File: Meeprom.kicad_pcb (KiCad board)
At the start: 2 copper layers, 16 x 38 mm, 4 parts, among them J1 Tandy_100_102_200_option_rom, U1 28C256

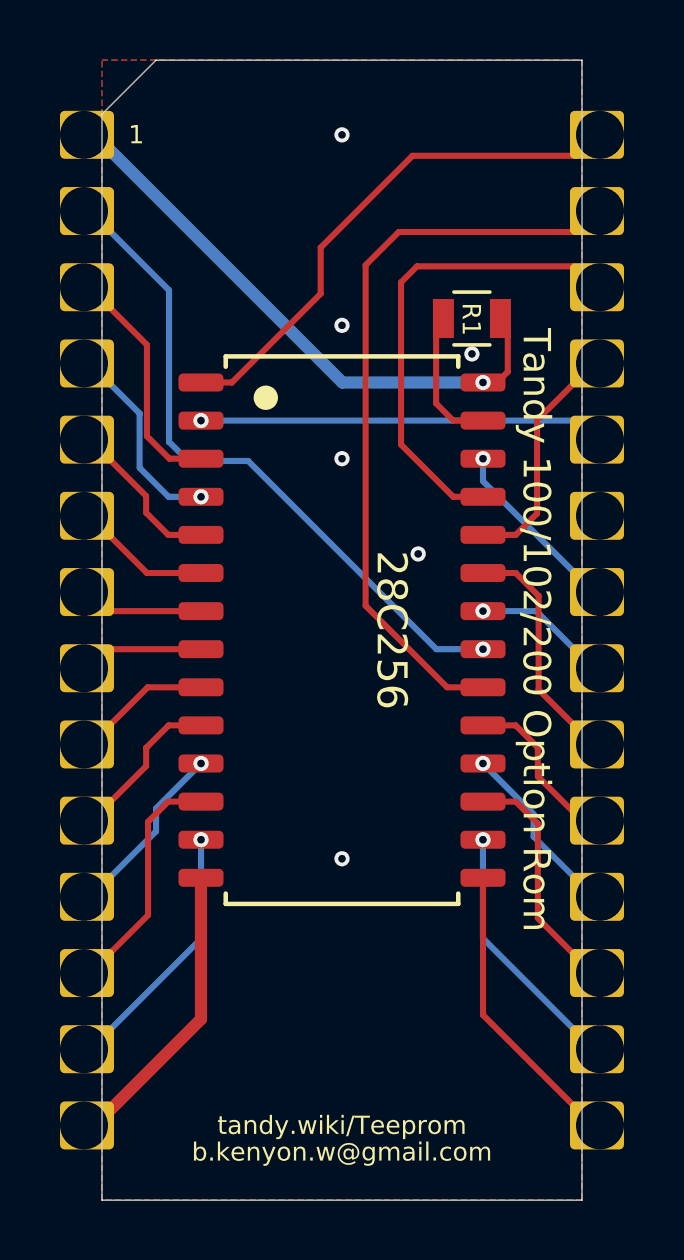
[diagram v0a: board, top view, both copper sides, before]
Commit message: Change license to CC. Add Meeprom. Add copper pours.
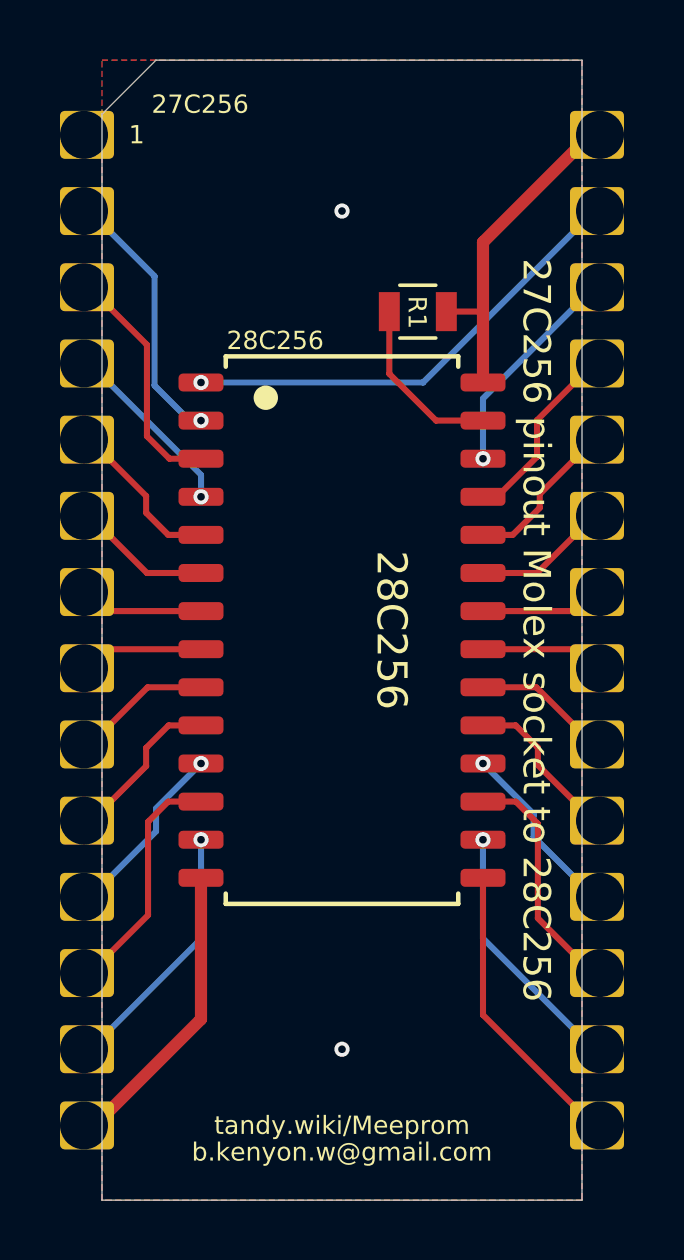
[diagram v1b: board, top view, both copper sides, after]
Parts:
- J1: value Tandy_100_102_200_option_rom -> Molex 8878 socket 27C256 pinout
- moved R1 1.82 mm to (149.7, 88.6)
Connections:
- J1 pad 1: /VCC -> (no net)
- J1 pad 2: /A10 -> /A12
- J1 pad 20: /A11 -> /~CE
- J1 pad 21: /~OE -> /A10
- J1 pad 22: /A13 -> /~OE
- J1 pad 23: (no net) -> /A11
- J1 pad 24: /A12 -> /A9
- J1 pad 25: /A9 -> /A8
- J1 pad 26: /A8 -> /A13
- J1 pad 27: /~CE -> /A14
- J1 pad 28: /A14 -> /VCC
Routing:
- net /~CE: track 24.9 -> 4.69 mm
- net /A10: track 22.2 -> 4.16 mm, vias 1 -> 0
- net /A8: track 15.9 -> 6.36 mm
- net /VCC: track 19.6 -> 11.3 mm, vias 1 -> 0
- net /A12: track 13.5 -> 8.93 mm
- net /A11: track 8.01 -> 4.69 mm
- net /A14: track 17.5 -> 15.7 mm, vias 0 -> 1
- net /A9: track 8.00 -> 6.38 mm
- net /A13: track 6.09 -> 7.44 mm
- net /~WE: track 4.73 -> 5.84 mm
- net /A6: track 6.71 -> 6.08 mm
- net /~OE: track 4.53 -> 4.16 mm, vias 1 -> 0
- net /VSS: vias 6 -> 2
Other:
- board text added: "27C256"
- board text added: "27C256 pinout Molex socket to 28C256"
- board text added: "28C256"
- board text added: "tandy.wiki/Meeprom"
- board text removed: "Tandy 100/102/200 Option Rom"
- board text removed: "tandy.wiki/Teeprom"

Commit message: improve ground paths in pours
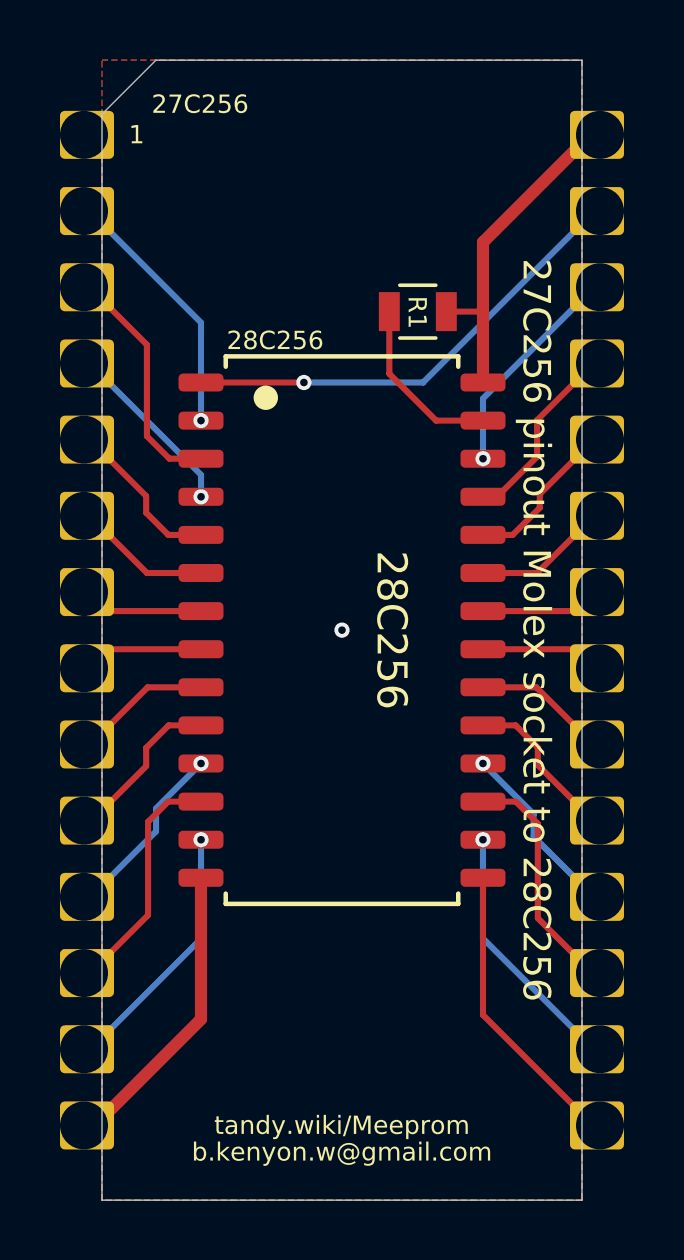
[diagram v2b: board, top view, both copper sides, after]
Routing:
- net /VSS: vias 2 -> 1
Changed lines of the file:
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@@
     (thickness 1.6)
     (drawings 13)
-    (tracks 116)
+    (tracks 114)
     (zones 0)
     (modules 4)
@@
     (add_net /~OE)
     (add_net /~WE)
-    (add_net "Net-(J1-Pad1)")
   )
   (module 000_LOCAL:pcb2molex8878_chamfer (layer Top)
@@
     (effects (font (size 0.6096 0.6096) (thickness 0.0762)) (justify left))
   )
-  (via (at 147.2184 113.157) (size 0.508) (drill 0.254) (layers Top Bottom) (net 27))
-  (via (at 147.2184 85.217) (size 0.508) (drill 0.254) (layers Top Bottom) (net 27))
   (segment (start 151.9184 112.015) (end 151.9184 107.442) (width 0.2032) (layer Top) (net 1))
   (segment (start 155.7274 115.697) (end 155.6004 115.697) (width 0.2032) (layer Top) (net 1))
@@
   (via (at 142.5184 92.202) (size 0.508) (drill 0.254) (layers Top Bottom) (net 18))
   (segment (start 138.7983 85.217) (end 138.6184 85.217) (width 0.2032) (layer Bottom) (net 18))
-  (segment (start 140.97 91.0336) (end 140.97 87.3887) (width 0.2032) (layer Bottom) (net 18))
-  (segment (start 140.97 87.3887) (end 138.7983 85.217) (width 0.2032) (layer Bottom) (net 18))
-  (segment (start 142.5184 92.202) (end 142.1384 92.202) (width 0.2032) (layer Bottom) (net 18))
-  (segment (start 142.1384 92.202) (end 140.97 91.0336) (width 0.2032) (layer Bottom) (net 18))
-  (segment (start 155.0924 92.202) (end 155.7274 92.837) (width 0.2032) (layer Bottom) (net 20))
+  (segment (start 142.5184 92.202) (end 142.5184 88.9371) (width 0.2032) (layer Bottom) (net 18))
+  (segment (start 142.5184 88.9371) (end 138.7983 85.217) (width 0.2032) (layer Bottom) (net 18))
   (via (at 142.5194 103.632) (size 0.508) (drill 0.254) (layers Top Bottom) (net 19))
   (segment (start 141.0208 105.1306) (end 142.5194 103.632) (width 0.2032) (layer Bottom) (net 19))
@@
   (segment (start 141.0208 105.8926) (end 141.0208 105.1306) (width 0.2032) (layer Bottom) (net 19))
   (segment (start 138.8364 108.077) (end 141.0208 105.8926) (width 0.2032) (layer Bottom) (net 19))
+  (segment (start 155.0924 92.202) (end 155.7274 92.837) (width 0.2032) (layer Bottom) (net 20))
   (segment (start 155.6258 92.837) (end 155.8184 92.837) (width 0.2032) (layer Top) (net 20))
   (segment (start 151.9184 96.012) (end 152.908 96.012) (width 0.2032) (layer Top) (net 20))
@@
   (segment (start 151.9184 101.092) (end 153.6954 101.092) (width 0.2032) (layer Top) (net 24))
   (segment (start 153.6954 101.092) (end 155.6004 102.997) (width 0.2032) (layer Top) (net 24))
-  (via (at 142.5184 90.932) (size 0.508) (drill 0.254) (layers Top Bottom) (net 25))
+  (segment (start 149.9235 90.932) (end 155.6385 85.217) (width 0.2032) (layer Bottom) (net 25))
+  (segment (start 145.9484 90.932) (end 149.9235 90.932) (width 0.2032) (layer Bottom) (net 25))
   (segment (start 155.6385 85.217) (end 155.8184 85.217) (width 0.2032) (layer Bottom) (net 25))
-  (segment (start 142.5184 90.932) (end 149.9235 90.932) (width 0.2032) (layer Bottom) (net 25))
-  (segment (start 149.9235 90.932) (end 155.6385 85.217) (width 0.2032) (layer Bottom) (net 25))
+  (via (at 145.9484 90.932) (size 0.508) (drill 0.254) (layers Top Bottom) (net 25))
+  (segment (start 142.5184 90.932) (end 145.9484 90.932) (width 0.2032) (layer Top) (net 25))
   (segment (start 151.9184 92.202) (end 150.3553 92.202) (width 0.2032) (layer Top) (net 26))
   (segment (start 148.7957 90.6424) (end 148.7957 88.5698) (width 0.2032) (layer Top) (net 26))
@@
   (segment (start 138.7094 115.697) (end 138.9761 115.697) (width 0.4064) (layer Top) (net 27))
   (segment (start 138.9761 115.697) (end 142.5184 112.1547) (width 0.4064) (layer Top) (net 27))
+  (via (at 147.2184 99.187) (size 0.508) (drill 0.254) (layers Top Bottom) (net 27))
   (segment (start 150.6967 88.5708) (end 150.6957 88.5698) (width 0.2032) (layer Top) (net 28))
   (segment (start 155.4988 82.677) (end 155.8184 82.677) (width 0.4064) (layer Top) (net 28))
